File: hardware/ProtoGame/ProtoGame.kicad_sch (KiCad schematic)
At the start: 22 parts, among them SW1 SW_DPST_x2, SW10 SW_MEC_5E, SW2 SW_MEC_5E, SW3 SW_MEC_5E, SW4 SW_MEC_5E, SW5 SW_MEC_5E, SW6 SW_MEC_5E, SW7 SW_MEC_5E, SW8 SW_MEC_5E, SW9 SW_MEC_5E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

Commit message: ADD SDCARD MODULE, LCD and Buzzer circuit and Power Supply circuit
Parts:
- added BT1: Battery, symbol Device:Battery
- added C1: 10uF, symbol Device:C_Polarized
- added J1: SD_Card_Module, symbol SDCARD_MODULE:SD_Card_Module
- added R10, R11: 10K, symbol Device:R
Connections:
- net +3.3V: now also R10.2, R11.1; no longer LCD1.2 (VCC)
- net Buz: now also C1.1
- net GND: now also U1.23 (VSS), U1.35 (VSS), U1.47 (VSS), U1.8 (VSSA), BT1.2 (-), C1.2, J1.3 (GND)
- net SCL-LCD: now also R11.2
- net SDA-LCD: now also R10.1
- net at SW1.1 (A): now also BT1.1 (+)
- net +3V0: now reaches SW1.2 (B)
- net +3V0: now also LCD1.2 (VCC), J1.4 (VCC)
- new net SD - CS: J1.7 (CS)
- new net SD - MISO: J1.1 (MISO)
- new net SD - MOSI: J1.9 (MOSI)
- new net SD - SCK: J1.8 (SCK)
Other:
- moved on the sheet: BZ1, SW1A, U1

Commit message: Update schemmatic
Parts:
- removed LCD1: OLED 128X32, symbol LCD_Oled:LCD
- removed U1: STM32F103C6Tx - MODULE, Package_QFP:LQFP-48_7x7mm_P0.5mm, symbol MCU_ST_STM32F1:STM32F103C6Tx
- added C2, C4, C5, C6, C9: 100nF, symbol Device:C
- added C3: 47uF, symbol Device:C
- added C7, C8: 4.7uF, symbol Device:C
- added LCD_Nokia1: 5110, symbol LCD_NOKIA-5110:LCD_Nokia_5110
- added U1: STM32F103C8Tx - MODULE, Package_QFP:LQFP-48_7x7mm_P0.5mm, symbol MCU_ST_STM32F1:STM32F103C8Tx
- added U2: AMS1117-3.3, Package_TO_SOT_SMD:SOT-223-3_TabPin2, symbol Regulator_Linear:AMS1117-3.3
- C1: value 10uF -> 100nF
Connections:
- net +3.3V: now also SW1.1 (A), C2.1, C7.1, U1.1 (VBAT), U1.24 (VDD), U1.36 (VDD), U1.48 (VDD), U1.9 (VDDA); no longer R10.2, R11.1
- net +3V0: no longer J1.4 (VCC), SW1.2 (B)
- net GND: now also C2.2, C3.2, C7.2, C9.2, U1.23 (VSS), U1.35 (VSS), U1.47 (VSS), U1.8 (VSSA), U2.1 (GND); no longer J1.3 (GND)
- net SD - CS: now also R10.2
- net at BT1.1 (+): now also U2.3 (VI); no longer SW1.1 (A)
- net SCL-LCD: no longer names the net of R11.2
- net SCL-LCD: now also C4.1, LCD_Nokia1.6 (VCC)
- net SD - MISO renamed MISO
- net SD - MOSI renamed MOSI
- net MOSI: now also LCD_Nokia1.4 (Din)
- net SDA-LCD: no longer names the net of R10.1
- net SDA-LCD: now also J1.4 (VCC), C5.1
- new net: C3.1, C9.1, SW1.2 (B), U2.2 (VO)
- new net: C4.2, LCD_Nokia1.8 (GND)
- new net: C5.2, J1.3 (GND)
- new net LCD - BL: LCD_Nokia1.7 (BL)
- new net LCD - CE: LCD_Nokia1.2 (CE), R11.1
- new net LCD - CLK: LCD_Nokia1.5 (CLK)
- new net LCD - DC: LCD_Nokia1.3 (DC)
- new net LCD - RST: LCD_Nokia1.1 (RST)
- no-connect marks 9 -> 11
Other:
- note added: "3X3 MATRIX PUSHBUTTONS CIRCUIT"
- note added: "BUZZER CIRCUIT"
- note added: "MCU"
- note added: "POWER SUPPLY CIRCUIT"
- note added: "SPI PROTOCOL COMUNICATION CIRCUIT"
- moved on the sheet: BT1, BZ1, C1, J1, R1, R2, R3, R4, R5, R6, R7, R8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

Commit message: Update schematic
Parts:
- removed BT1: Battery, symbol Device:Battery
- added BT1: Battery_Cell, symbol Device:Battery_Cell
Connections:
- net GND: now also BT1.2 (-)
- net at U2.3 (VI): now also BT1.1 (+)
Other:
- moved on the sheet: BZ1, C1, C3, C9, SW1A, U2

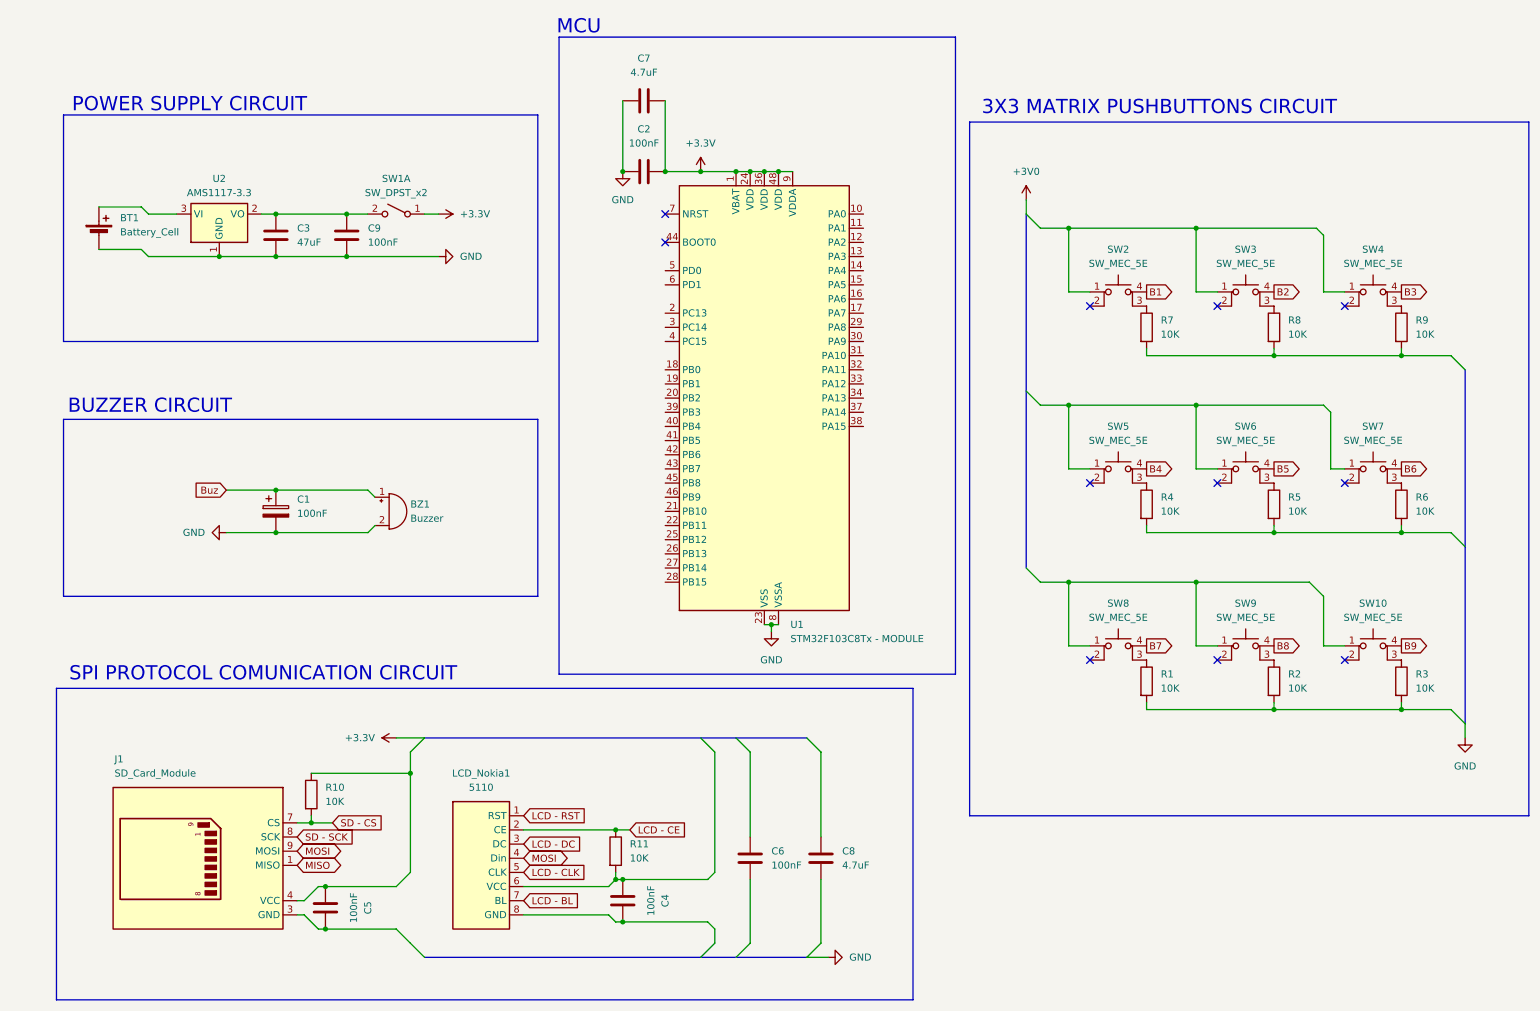
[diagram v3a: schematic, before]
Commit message: Add MCU Pinout
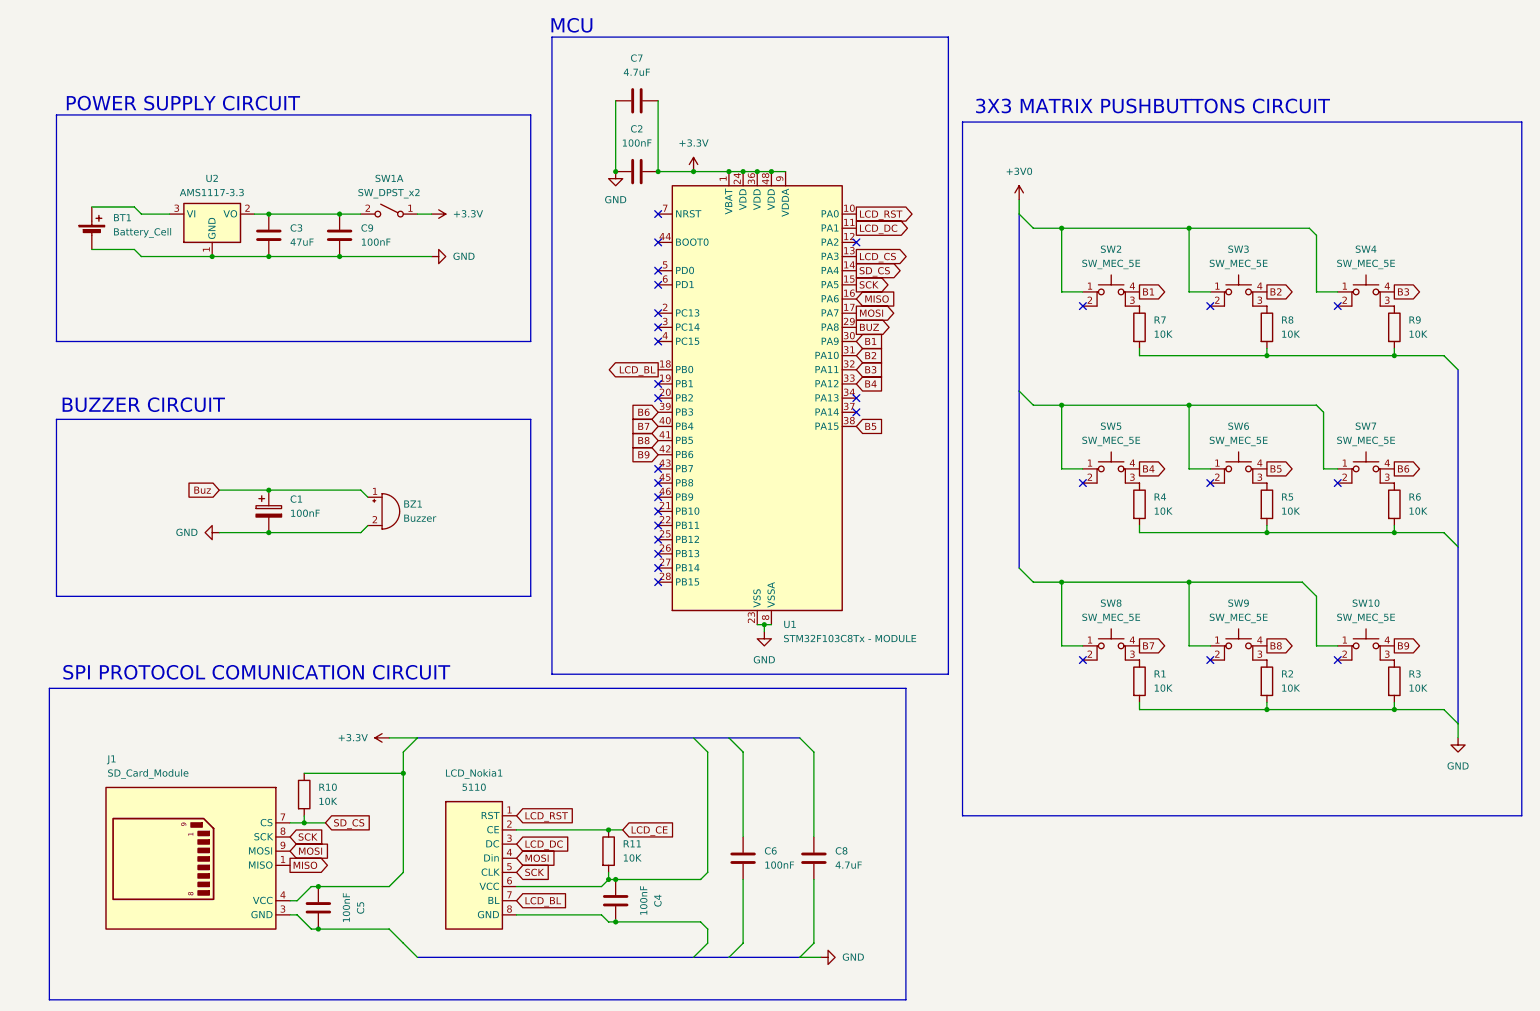
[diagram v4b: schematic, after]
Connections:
- net LCD - BL is gone; now on net LCD_BL: LCD_Nokia1.7 (BL)
- net LCD - CLK is gone; now on net SCK: LCD_Nokia1.5 (CLK)
- net LCD - DC is gone; now on net LCD_DC: LCD_Nokia1.3 (DC)
- net LCD - RST is gone; now on net LCD_RST: LCD_Nokia1.1 (RST)
- net SD - CS is gone; now on net SD_CS: J1.7 (CS), R10.2
- net SD - SCK is gone; now on net SCK: J1.8 (SCK)
- net B1: now also U1.30 (PA9)
- net B2: now also U1.31 (PA10)
- net B3: now also U1.32 (PA11)
- net B4: now also U1.33 (PA12)
- net B5: now also U1.38 (PA15)
- net B6: now also U1.39 (PB3)
- net B7: now also U1.40 (PB4)
- net B8: now also U1.41 (PB5)
- net B9: now also U1.42 (PB6)
- net MISO: now also U1.16 (PA6)
- net MOSI: now also U1.17 (PA7)
- net LCD_RST: now reaches U1.10 (PA0)
- net LCD_DC: now reaches U1.11 (PA1)
- net LCD_CS: now reaches U1.13 (PA3)
- net SD_CS: now reaches U1.14 (PA4)
- net SCK: now reaches U1.15 (PA5)
- net LCD_BL: now reaches U1.18 (PB0)
- net BUZ: now reaches U1.29 (PA8)
- net LCD - CE renamed LCD_CE
- no-connect marks 11 -> 30
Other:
- moved on the sheet: BT1, BZ1, C1, C2, C3, C4, C5, C6, C7, C8, C9, J1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

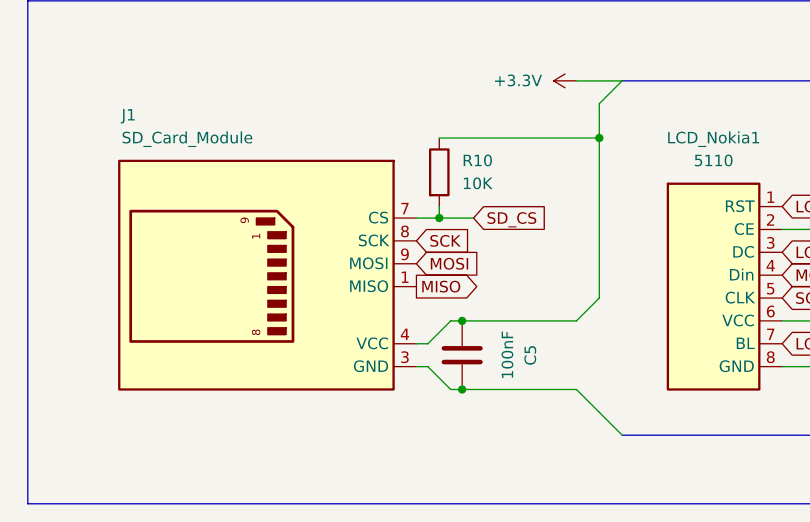
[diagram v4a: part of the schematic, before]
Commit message: Add the footprints and 3D models for ProtoGame PCI and add the png assets v0
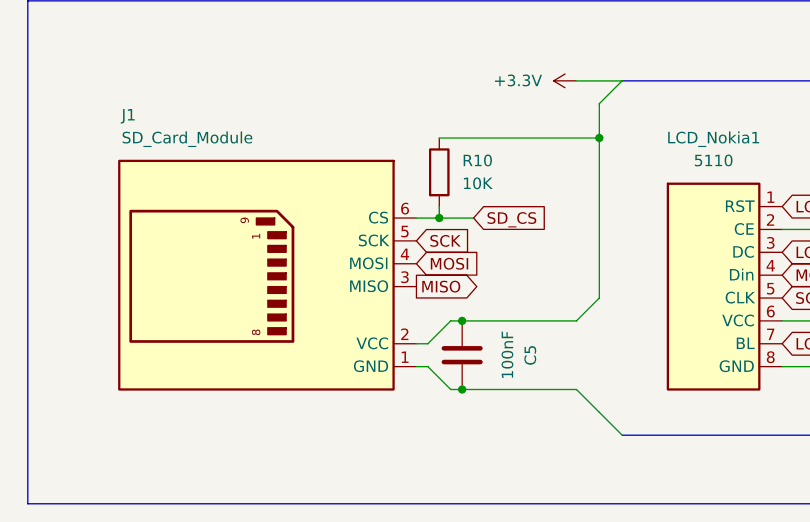
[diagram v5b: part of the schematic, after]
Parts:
- BT1: footprint (none) -> Battery:BatteryHolder_Keystone_1042_1x18650
- BZ1: footprint (none) -> Buzzer_Beeper:Buzzer_12x9.5RM7.6
- C1, C2, C4, C5, C6, C9: footprint (none) -> Capacitor_THT:C_Disc_D5.0mm_W2.5mm_P2.50mm
- C3, C7, C8: footprint (none) -> Capacitor_THT:C_Disc_D3.0mm_W2.0mm_P2.50mm
- J1: footprint (none) -> microsd:microsd_module
- LCD_Nokia1: footprint (none) -> nokia_5110:PinSocket_1x08_P2.54mm_Vertical
- R1, R10, R11, R2, R3, R4, R5, R6, R7, R8, R9: footprint (none) -> Resistor_THT:R_Axial_DIN0207_L6.3mm_D2.5mm_P7.62mm_Horizontal
- SW1: footprint (none) -> slidesw:SW_EG1213
- SW10, SW2, SW3, SW4, SW5, SW6, SW7, SW8, SW9: footprint (none) -> Button_Switch_THT:SW_PUSH-12mm_Wuerth-430476085716
- U1: footprint Package_QFP:LQFP-48_7x7mm_P0.5mm -> STM32:MODULE_ZC323000-with-pinholder
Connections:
- net MISO: now also J1.3 (MISO); no longer J1.1 (MISO)
- net MOSI: now also J1.4 (MOSI); no longer J1.9 (MOSI)
- net SCK: now also J1.5 (SCK); no longer J1.8 (SCK)
- net SD_CS: now also J1.6 (VSS); no longer J1.7 (CS)
- net at C5.1, R10.1: now also J1.2 (VCC); no longer J1.4 (VCC)
- net at C5.2: now also J1.1 (GND); no longer J1.3 (GND)

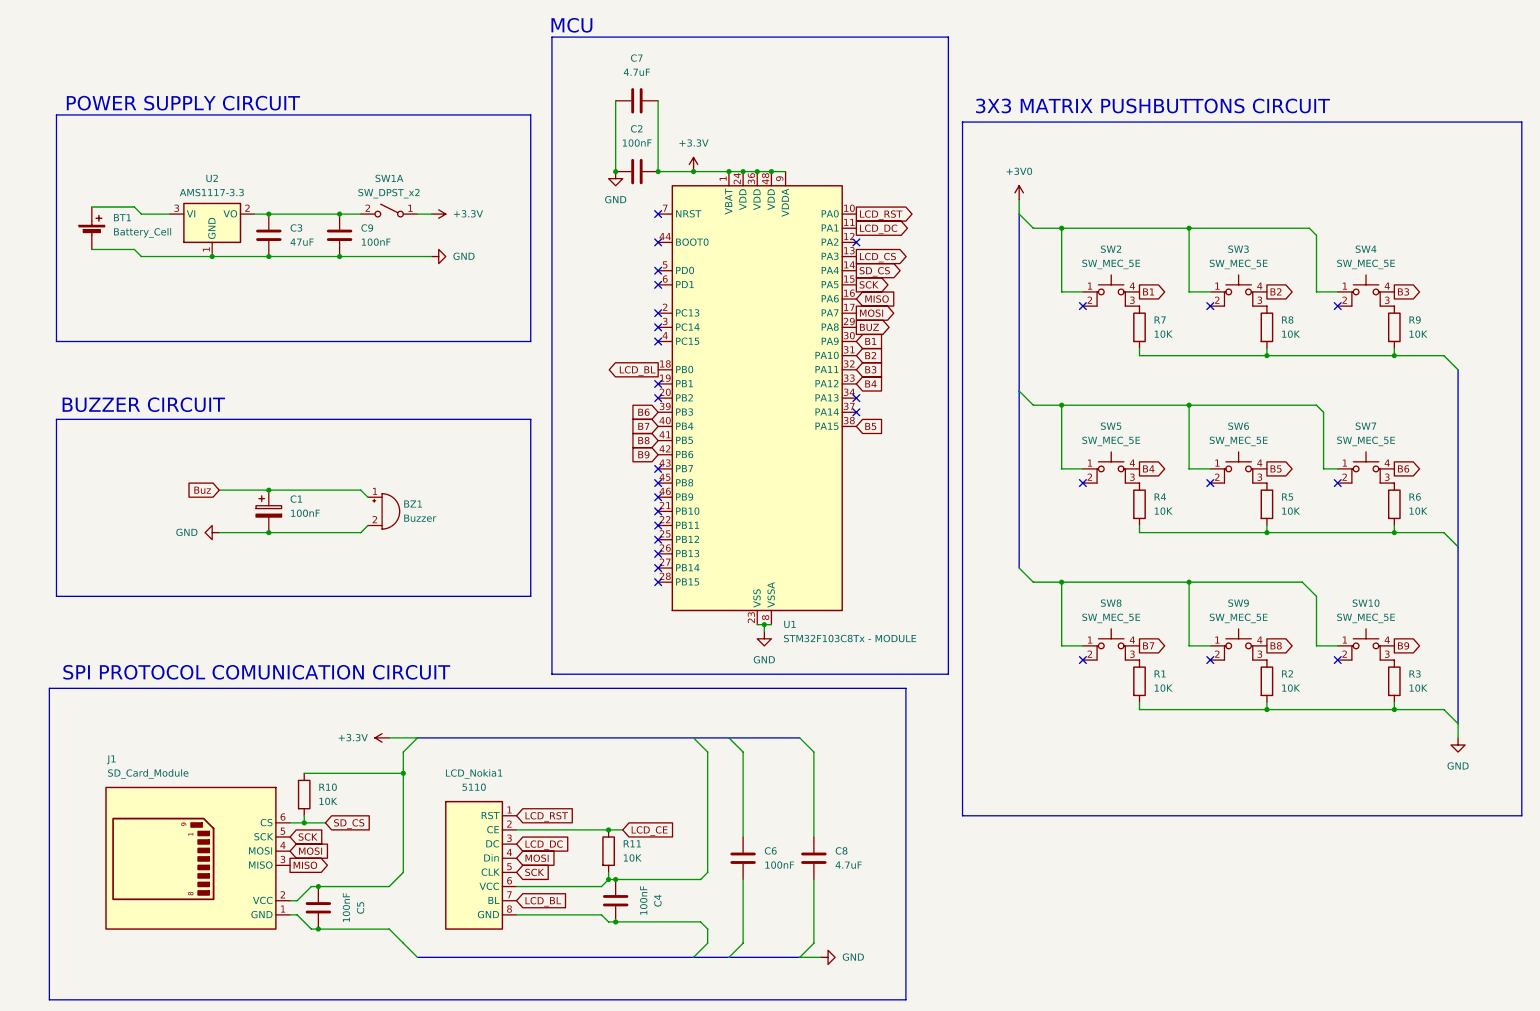
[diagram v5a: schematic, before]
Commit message: ProtoGame v2 its complete and with new design, add assets images: footprint and 3d model
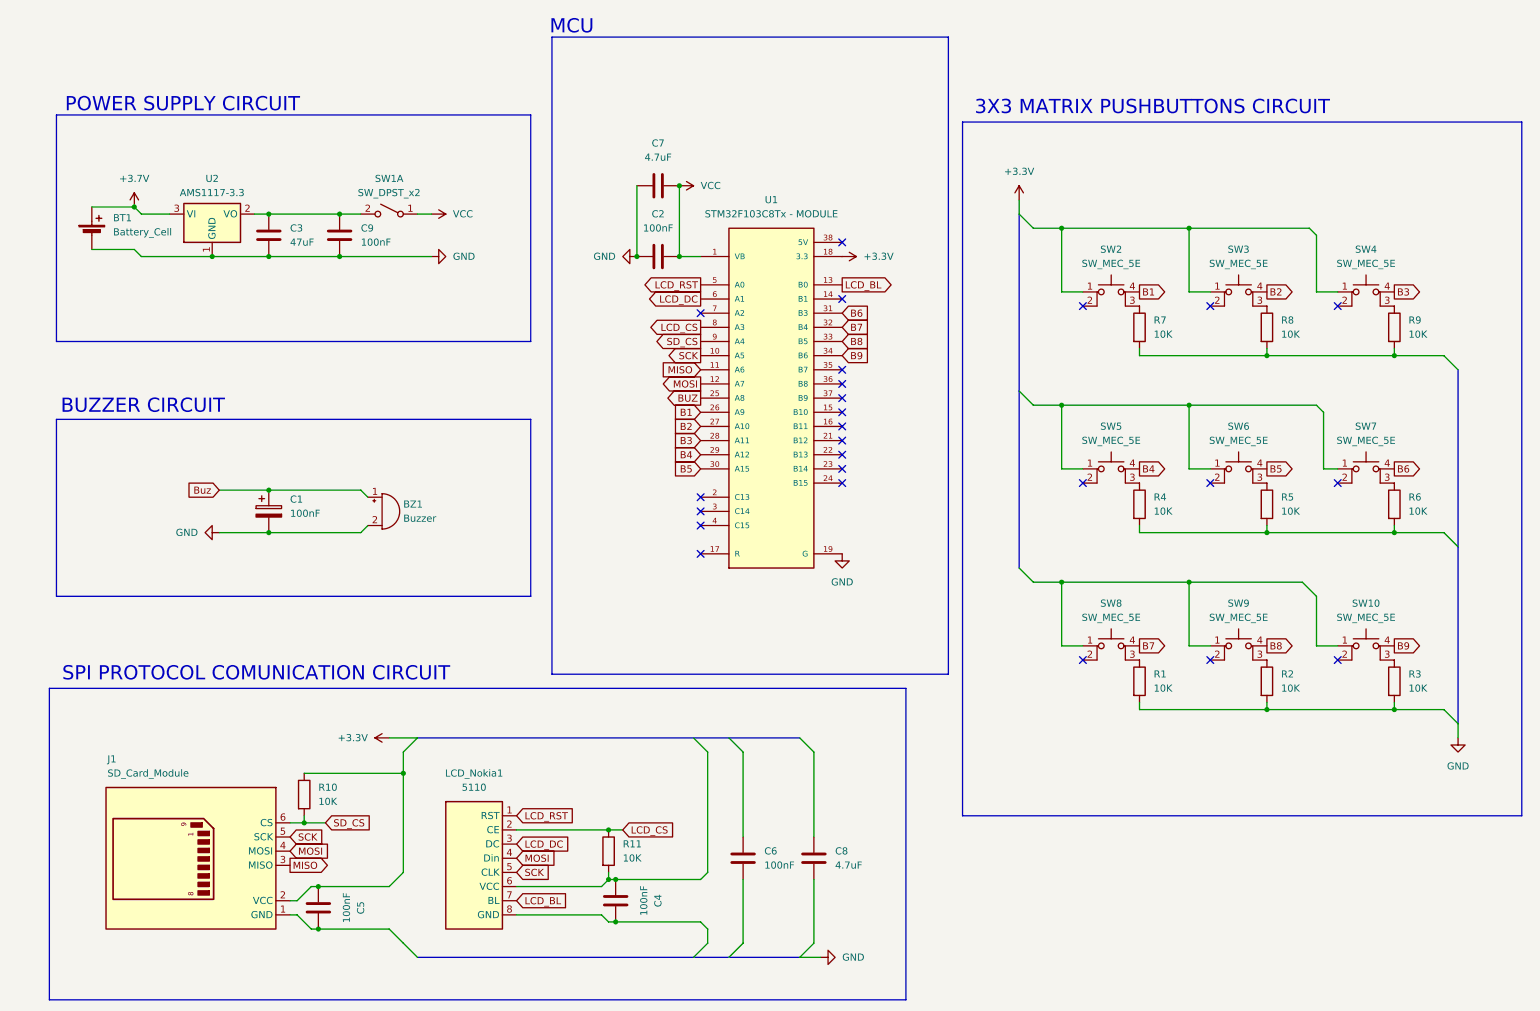
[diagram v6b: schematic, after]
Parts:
- BT1: footprint Battery:BatteryHolder_Keystone_1042_1x18650 -> Connector_JST:JST_EH_B2B-EH-A_1x02_P2.50mm_Vertical
- C1: footprint Capacitor_THT:C_Disc_D5.0mm_W2.5mm_P2.50mm -> Capacitor_THT:C_Radial_D5.0mm_H5.0mm_P2.00mm
- U1: symbol MCU_ST_STM32F1:STM32F103C8Tx -> ZC323000:ZC323000; Availability (none) -> Not in stock; Check_prices (none) -> https://www.snapeda.com/parts/ZC323000/YKS/view-part/?ref=e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; Description_1 (none) -> STM32F103C8T6 ARM STM32 Minimum System Development Board Mo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; MANUFACTURER (none) -> YKS; MAXIMUM_PACKAGE_HEIGHT (none) -> N/A; MF (none) -> YKS; MP (none) -> ZC323000; PARTREV (none) -> N/A; Package (none) -> None; Price (none) -> None; STANDARD (none) -> Manufacturer Recommendations; SnapEDA_Link (none) -> https://www.snapeda.com/parts/ZC323000/YKS/view-part/?ref=s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
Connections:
- net LCD_CE is gone; now on net LCD_CS: LCD_Nokia1.2 (CE), R11.1
- net +3.3V: now also U1.18 (3.3), U1.40 (3.3); no longer C2.1, C7.1, SW1.1 (A), U1.1 (VBAT), U1.24 (VDD), U1.36 (VDD), U1.48 (VDD), U1.9 (VDDA)
- net B1: now also U1.26 (A9); no longer U1.30 (PA9)
- net B2: now also U1.27 (A10); no longer U1.31 (PA10)
- net B3: now also U1.28 (A11); no longer U1.32 (PA11)
- net B4: now also U1.29 (A12); no longer U1.33 (PA12)
- net B5: now also U1.30 (A15); no longer U1.38 (PA15)
- net B6: now also U1.31 (B3); no longer U1.39 (PB3)
- net B7: now also U1.32 (B4); no longer U1.40 (PB4)
- net B8: now also U1.33 (B5); no longer U1.41 (PB5)
- net B9: now also U1.34 (B6); no longer U1.42 (PB6)
- net BUZ: now also U1.25 (A8); no longer U1.29 (PA8)
- net LCD_BL: now also U1.13 (B0); no longer U1.18 (PB0)
- net LCD_CS: now also U1.8 (A3); no longer U1.13 (PA3)
- net LCD_DC: now also U1.6 (A1); no longer U1.11 (PA1)
- net LCD_RST: now also U1.5 (A0); no longer U1.10 (PA0)
- net MISO: now also U1.11 (A6); no longer U1.16 (PA6)
- net MOSI: now also U1.12 (A7); no longer U1.17 (PA7)
- net SCK: now also U1.10 (A5); no longer U1.15 (PA5)
- net SD_CS: now also U1.9 (A4); no longer U1.14 (PA4)
- net G: now reaches U1.19 (G)
- net G: now also BT1.2 (-), BZ1.2 (-), C1.2, C2.2, C3.2, C7.2, C9.2, U1.20 (G), U1.39 (G), U2.1 (GND)
- net +3.7V: now reaches BT1.1 (+), U2.3 (VI)
- removed net GND: BT1.2 (-), BZ1.2 (-), C1.2, C2.2, C3.2, C7.2, C9.2, U1.23 (VSS), U1.35 (VSS), U1.47 (VSS), U1.8 (VSSA), U2.1 (GND)
- new net VCC: C2.1, C7.1, SW1.1 (A), U1.1 (VB)
- no-connect marks 30 -> 25
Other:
- moved on the sheet: C2, C7
